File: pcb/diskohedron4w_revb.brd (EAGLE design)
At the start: 87.2 x 54.7 mm, 23 parts

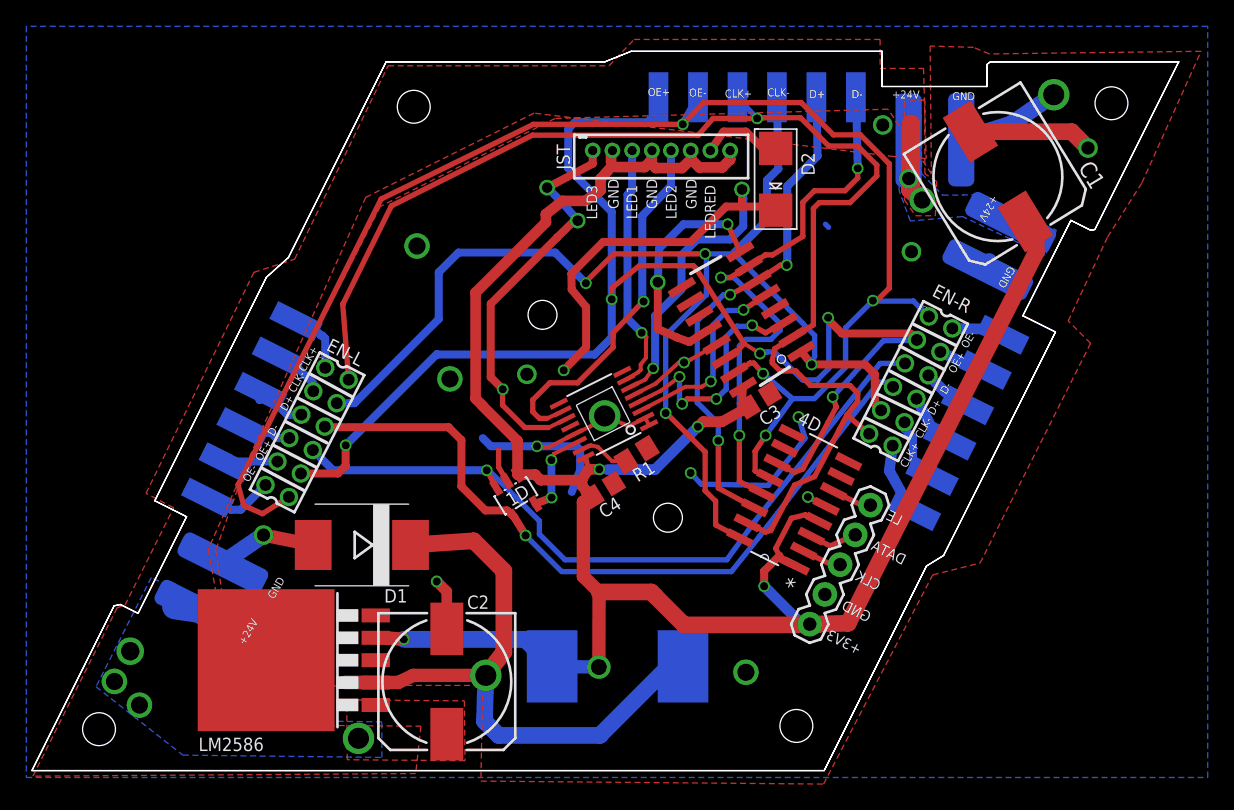
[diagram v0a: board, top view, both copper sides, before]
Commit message: first commit for rev.b after wrong hermaphrodite spotting
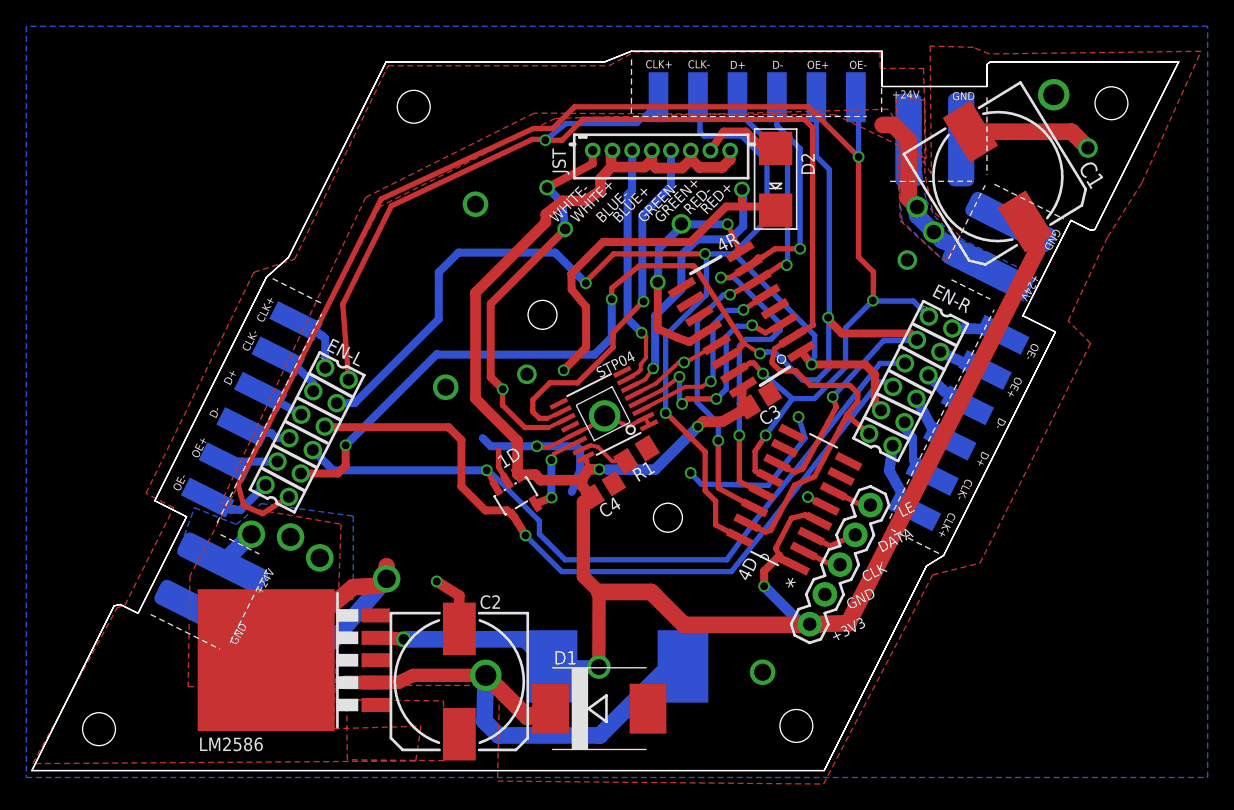
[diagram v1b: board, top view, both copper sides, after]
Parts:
- moved D1 21.9 mm to (43.2, 4.73), turned to 0 degrees
- moved C2 0.95 mm to (32.5, 6.79)
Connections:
- net +24V: now also U$12.P$1, U$6.P$1; no longer U$12.P$2, U$6.P$2
- net CLK+: now also IN1.P$6; no longer IN1.P$4
- net CLK-: now also IN1.P$5; no longer IN1.P$3
- net DATA+: now also IN1.P$4; no longer IN1.P$2
- net DATA-: now also IN1.P$3; no longer IN1.P$1
- net GND: now also U$12.P$2, U$6.P$2; no longer U$12.P$1, U$6.P$1
- net OE+: now also IN1.P$2; no longer IN1.P$6
- net OE-: now also IN1.P$1; no longer IN1.P$5
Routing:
- net N$2: track 50.9 -> 40.8 mm
- net +24V: track 10.5 -> 20.5 mm, vias 7 -> 5
- net GND: track 92.4 -> 100.6 mm, vias 16 -> 17
- net OE+: track 107.2 -> 101.5 mm
- net CLK-: track 98.2 -> 103.3 mm
- net DATA-: track 43.1 -> 41.3 mm
- net DATAOUT+L: track 5.28 -> 3.54 mm
- net CLK+: track 101.1 -> 102.3 mm
- net LED3: track 31.4 -> 30.6 mm
- net DATA+: track 38.8 -> 39.5 mm
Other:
- board text added: "06/2014"
- board text added: "4R"
- board text added: "BLUE+"
- board text added: "BLUE-"
- board text added: "GREEN+"
- board text added: "GREEN-"
- board text added: "RED+"
- board text added: "RED-"
- board text added: "STP04"
- board text added: "WHITE+"
- board text added: "WHITE-"
- board text added: "rev.B"
- board text removed: "05/2014"
- board text removed: "LED1"
- board text removed: "LED2"
- board text removed: "LED3"
- board text removed: "LEDRED"
- board text removed: "rev.A"

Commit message: changed output bridges to SMD pads, some cleanup, some labelling for bsilk
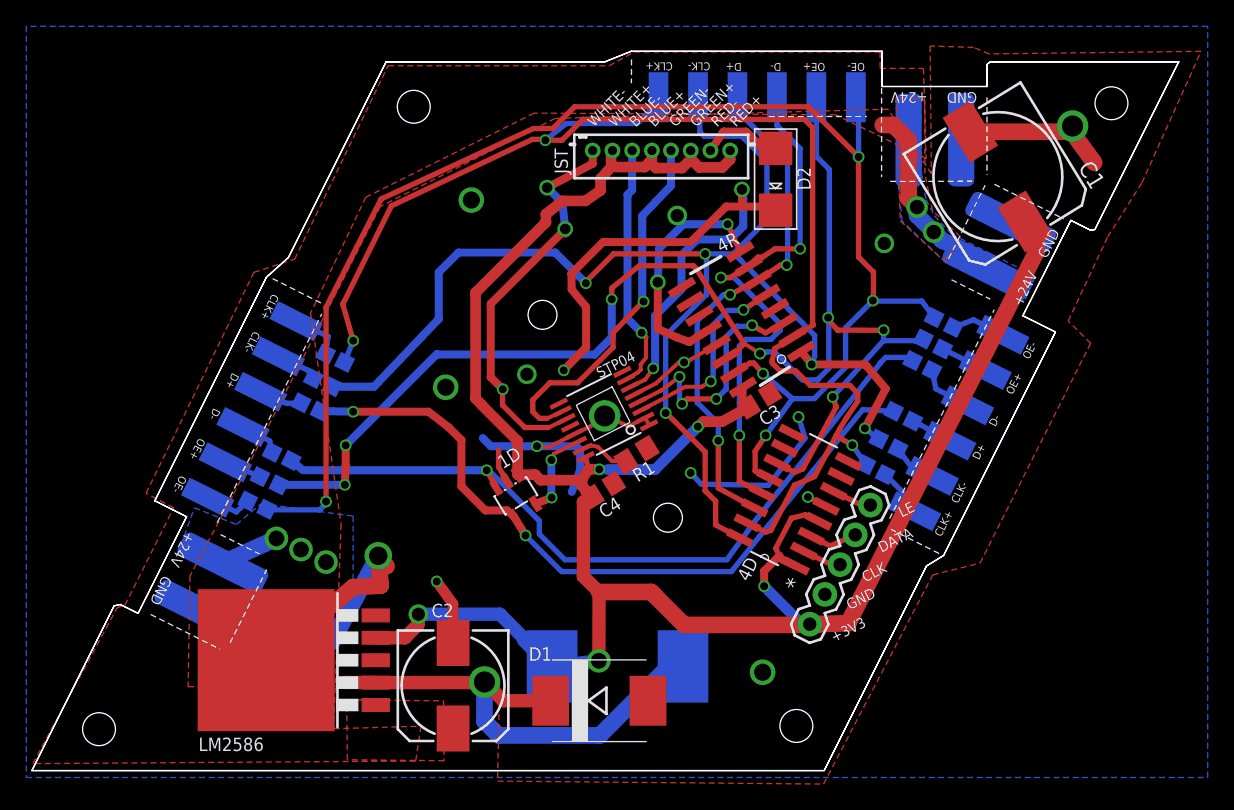
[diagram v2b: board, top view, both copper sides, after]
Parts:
- removed EN-L, EN-R: 87758-1216, con-molex:87758-1216
- added TP1, TP10, TP11, TP12, TP13, TP14, TP15, TP16, TP17, TP18, TP19, TP2, TP20, TP21, TP22, TP23, TP24, TP3, TP4, TP5, TP6, TP7, TP8, TP9: TPTP12SQ, testpad:TP12SQ
- C2: device rcl:153CLV-1010 -> rcl:153CLV-0810
- moved D1 0.60 mm to (43.2, 5.33)
- moved C2 0.57 mm to (32.0, 6.48)
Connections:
- net CLK+: now also TP13.TP, TP6.TP; no longer EN-L.2, EN-R.11
- net CLK+L: now also TP19.TP; no longer EN-L.1
- net CLK+R: now also TP12.TP; no longer EN-R.12
- net CLK-: now also TP14.TP, TP5.TP; no longer EN-L.4, EN-R.9
- net CLK-L: now also TP20.TP; no longer EN-L.3
- net CLK-R: now also TP11.TP; no longer EN-R.10
- net DATAOUT+: now also TP15.TP, TP4.TP; no longer EN-L.6, EN-R.7
- net DATAOUT+L: now also TP21.TP; no longer EN-L.5
- net DATAOUT+R: now also TP10.TP; no longer EN-R.8
- net DATAOUT-: now also TP16.TP, TP3.TP; no longer EN-L.8, EN-R.5
- net DATAOUT-L: now also TP22.TP; no longer EN-L.7
- net DATAOUT-R: now also TP9.TP; no longer EN-R.6
- net OE+: now also TP17.TP, TP2.TP; no longer EN-L.10, EN-R.3
- net OE+L: now also TP23.TP; no longer EN-L.9
- net OE+R: now also TP8.TP; no longer EN-R.4
- net OE-: now also TP1.TP, TP18.TP; no longer EN-L.12, EN-R.1
- net OE-L: now also TP24.TP; no longer EN-L.11
- net OE-R: now also TP7.TP; no longer EN-R.2
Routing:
- net GND: track 100.6 -> 105.0 mm, vias 17 -> 16
- net N$2: track 40.8 -> 37.0 mm
- net CLK-: track 103.3 -> 106.3 mm, vias 4 -> 5
- net CLK+L: track 6.32 -> 4.05 mm
- net CLK+R: track 5.95 -> 3.71 mm
- net DATAOUT-: track 57.8 -> 60.0 mm
- net CLK-R: track 5.46 -> 3.66 mm
- net OE-L: track 5.40 -> 3.63 mm
- net +3V3: track 172.0 -> 173.5 mm
- net OE+R: track 5.10 -> 3.60 mm
- net +24V: track 20.5 -> 21.9 mm
- net OE+: track 101.5 -> 102.8 mm, vias 5 -> 7
- net DATAOUT+R: track 4.23 -> 3.17 mm
- net OE+L: track 3.97 -> 3.02 mm
- net CLK-L: track 4.99 -> 4.09 mm
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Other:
- board text added: "OUT-L"
- board text added: "OUT-R"
- board text removed: "OUTPUT-L"
- board text removed: "OUTPUT-R"

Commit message: digital line driver and receiver swapped to bottom, major redesign
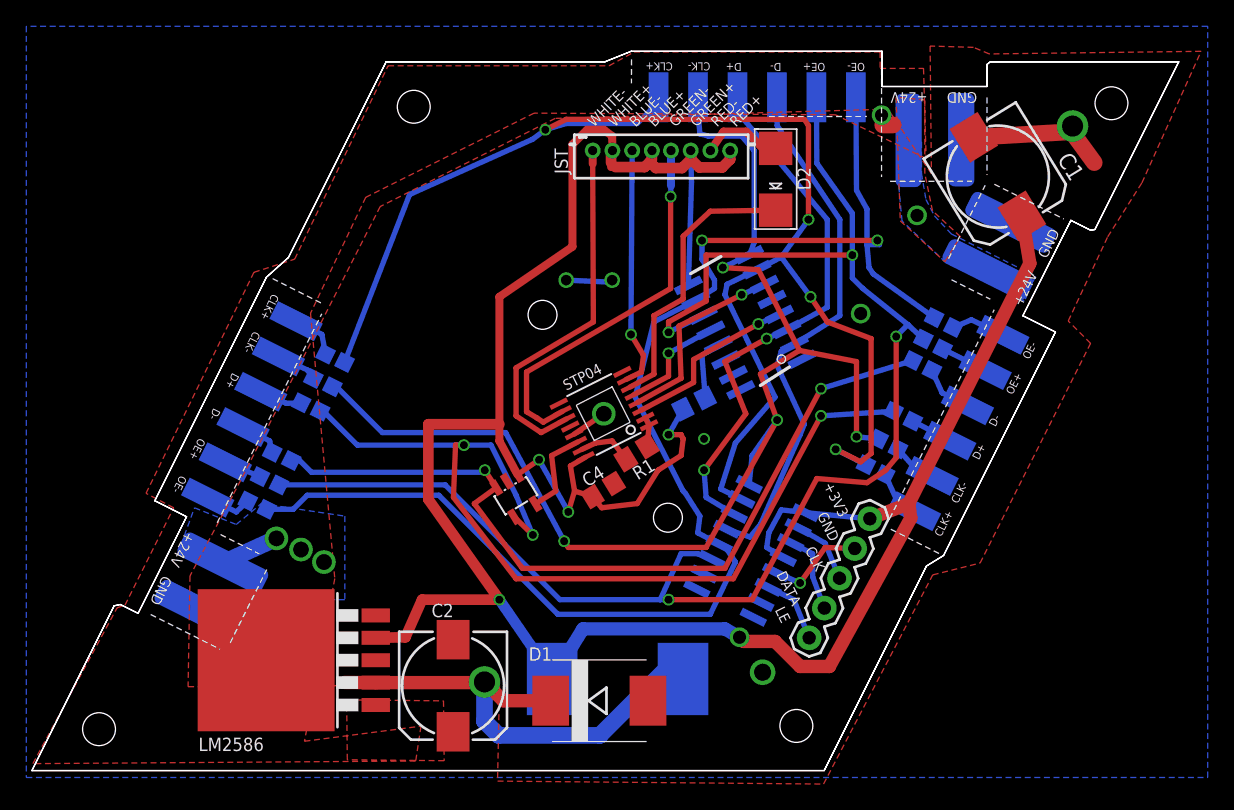
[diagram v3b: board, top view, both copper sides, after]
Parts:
- C1: device rcl:153CLV-1010 -> rcl:175TMP-0808
- C2: device rcl:153CLV-0810 -> rcl:175TMP-0808
- moved 4D 13.9 mm to (50.6, 13.8), flipped to the bottom, turned to 26.6 degrees
- moved JP1 9.23 mm to (63.7, 19.2), turned to 243 degrees
- moved C3 4.97 mm to (50.4, 27.9), flipped to the bottom, turned to 153.4 degrees
- moved L1 0.95 mm to (44.5, 6.99)
- moved 4R 0.35 mm to (54.2, 34.1), flipped to the bottom, turned to 243.4 degrees
- moved R1 0.16 mm to (46.0, 24.2)
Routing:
- net GND: track 105.0 -> 32.7 mm, vias 16 -> 8
- net +3V3: track 173.5 -> 201.3 mm
- net N$3: track 47.7 -> 21.6 mm, vias 3 -> 0
- net +24V: track 21.9 -> 5.28 mm
- net DATAOUT+: track 56.7 -> 72.1 mm, vias 2 -> 3
- net OE+: track 102.8 -> 116.9 mm, vias 7 -> 4
- net CLK+: track 102.2 -> 114.2 mm, vias 3 -> 4
- net CLK-: track 106.3 -> 98.4 mm, vias 5 -> 4
- net OE-: track 114.2 -> 106.8 mm, vias 5 -> 2
- net CLK: track 18.7 -> 15.0 mm, vias 4 -> 1
- net DATAOUT-: track 60.0 -> 63.1 mm, vias 1 -> 2
- net LED3: track 30.6 -> 28.0 mm, vias 3 -> 0
- net EXTDATA: track 3.71 -> 6.16 mm
- net EXTCLK: track 3.01 -> 5.25 mm
- net EXTOE: track 3.08 -> 5.28 mm
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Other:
- board text removed: "4R"

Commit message: cleanup rev.b swapped single line driver to bottom side
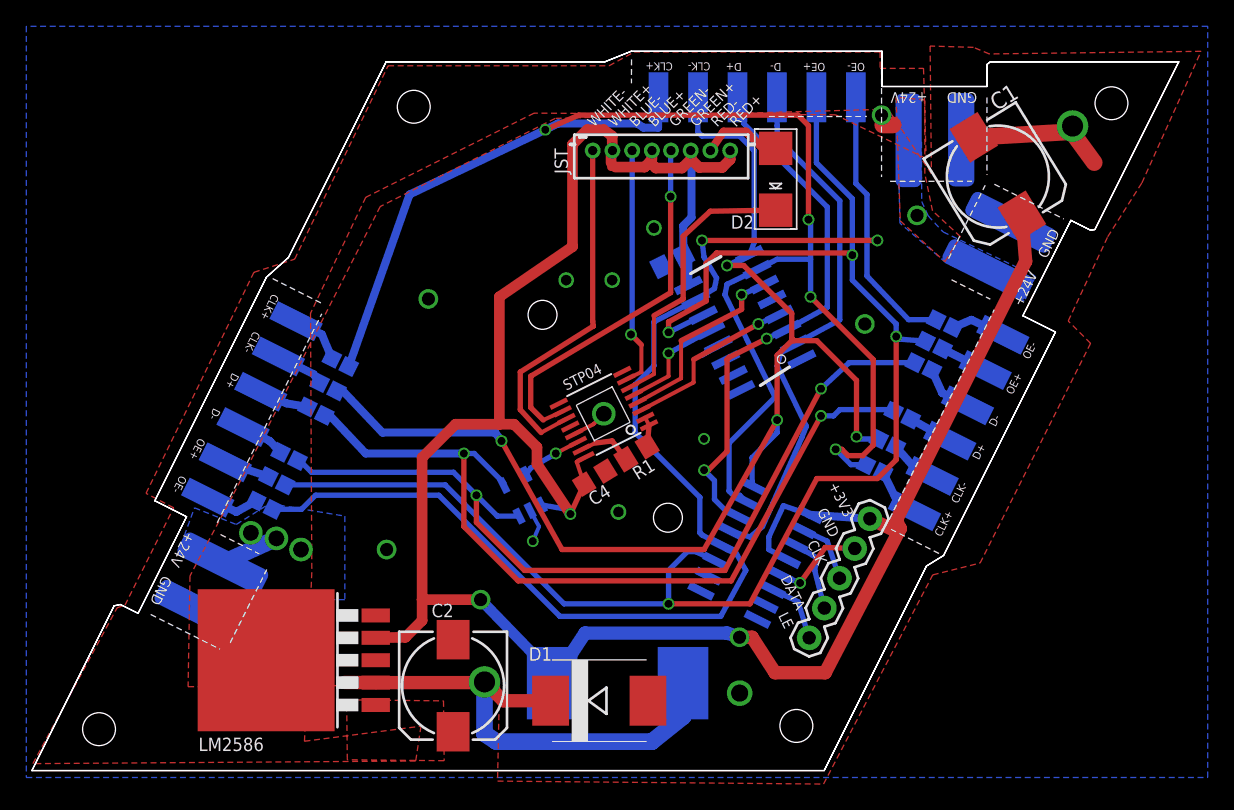
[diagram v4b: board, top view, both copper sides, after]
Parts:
- C1, C2: device rcl:175TMP-0808 -> rcl:175TMP-0810
- moved C3 11.0 mm to (48.7, 38.8), turned to 333.4 degrees
- moved C4 1.14 mm to (42.8, 22.3)
- moved TP22 0.64 mm to (18.9, 24.2)
- moved TP23 0.63 mm to (18.0, 22.4)
- moved TP24 0.63 mm to (17.1, 20.5)
- moved TP20 0.57 mm to (21.9, 29.5)
- moved TP21 0.57 mm to (21.0, 27.7)
- moved TP19 0.57 mm to (22.8, 31.4)
- moved 1D 0.51 mm to (37.3, 21.0), flipped to the bottom, turned to 333.4 degrees
- moved TP16 0.48 mm to (20.2, 23.6)
- moved TP17 0.48 mm to (19.3, 21.7)
- moved TP18 0.48 mm to (18.4, 19.9)
- moved TP13 0.45 mm to (24.1, 30.7)
- moved TP14 0.45 mm to (23.2, 28.9)
- moved TP15 0.45 mm to (22.3, 27.0)
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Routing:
- net +3V3: track 201.3 -> 185.4 mm, vias 5 -> 3
- net DATAOUT+: track 72.1 -> 63.6 mm, vias 3 -> 2
- net GND: track 32.7 -> 28.2 mm, vias 8 -> 13
- net N$2: track 37.4 -> 40.4 mm
- net OE-: track 106.8 -> 109.6 mm
- net CLK+: track 114.2 -> 116.5 mm
- net CLK-: track 98.4 -> 96.7 mm
- net DATAOUT-: track 63.1 -> 64.7 mm
- net DATAOUT: track 6.79 -> 5.18 mm, vias 0 -> 1
- net LED2: track 29.3 -> 28.5 mm
- net LED3: track 28.0 -> 27.3 mm
- net OE+L: track 3.02 -> 3.61 mm
- net CLK-L: track 4.09 -> 4.66 mm
- net DATA-: track 40.7 -> 41.3 mm
- net OE-L: track 3.63 -> 4.15 mm
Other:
- board text added: "*"

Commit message: further cleaning, added bottomlayer cream masks for smd bridges
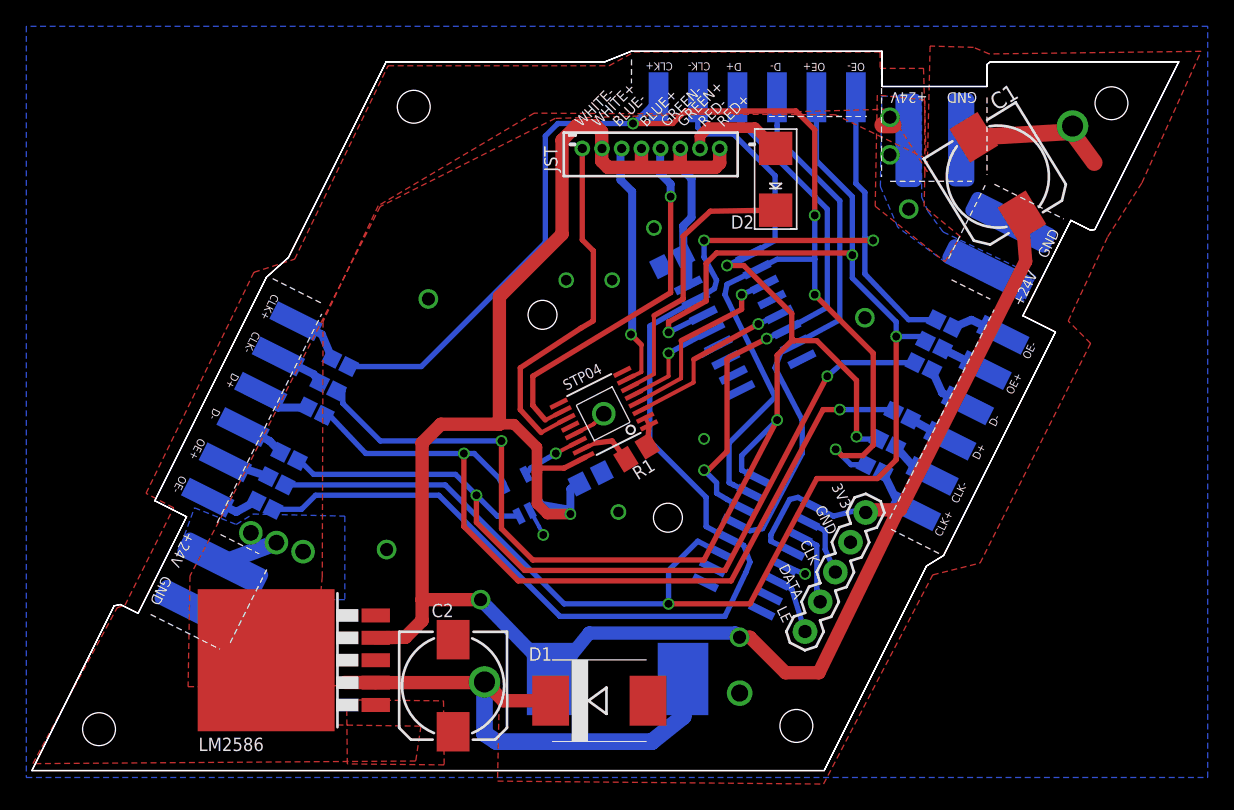
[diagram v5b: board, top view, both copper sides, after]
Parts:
- moved JST 0.81 mm to (44.1, 47.3)
- moved 4D 0.71 mm to (51.2, 14.3)
- moved JP1 0.57 mm to (63.4, 19.6)
- moved C4 0.33 mm to (42.5, 22.2), flipped to the bottom, turned to 153.4 degrees
- moved L1 0.32 mm to (44.5, 6.99)
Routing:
- net CLK+: track 116.5 -> 110.5 mm
- net GND: track 28.2 -> 22.2 mm
- net CLK-: track 96.7 -> 101.9 mm
- net LED0: track 6.24 -> 8.60 mm
- net +3V3: track 185.4 -> 187.0 mm
- net OE-: track 109.6 -> 108.5 mm
- net OE+: track 117.1 -> 118.2 mm
- net DATA+: track 41.4 -> 42.0 mm
- net LED1: track 18.5 -> 19.1 mm
- net +24V: track 5.28 -> 5.16 mm, vias 5 -> 6
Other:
- board text added: "3V3"
- board text removed: "+3V3"
